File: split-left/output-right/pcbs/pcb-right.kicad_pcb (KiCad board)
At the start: 2 copper layers, 243.1 x 138 mm, 113 parts

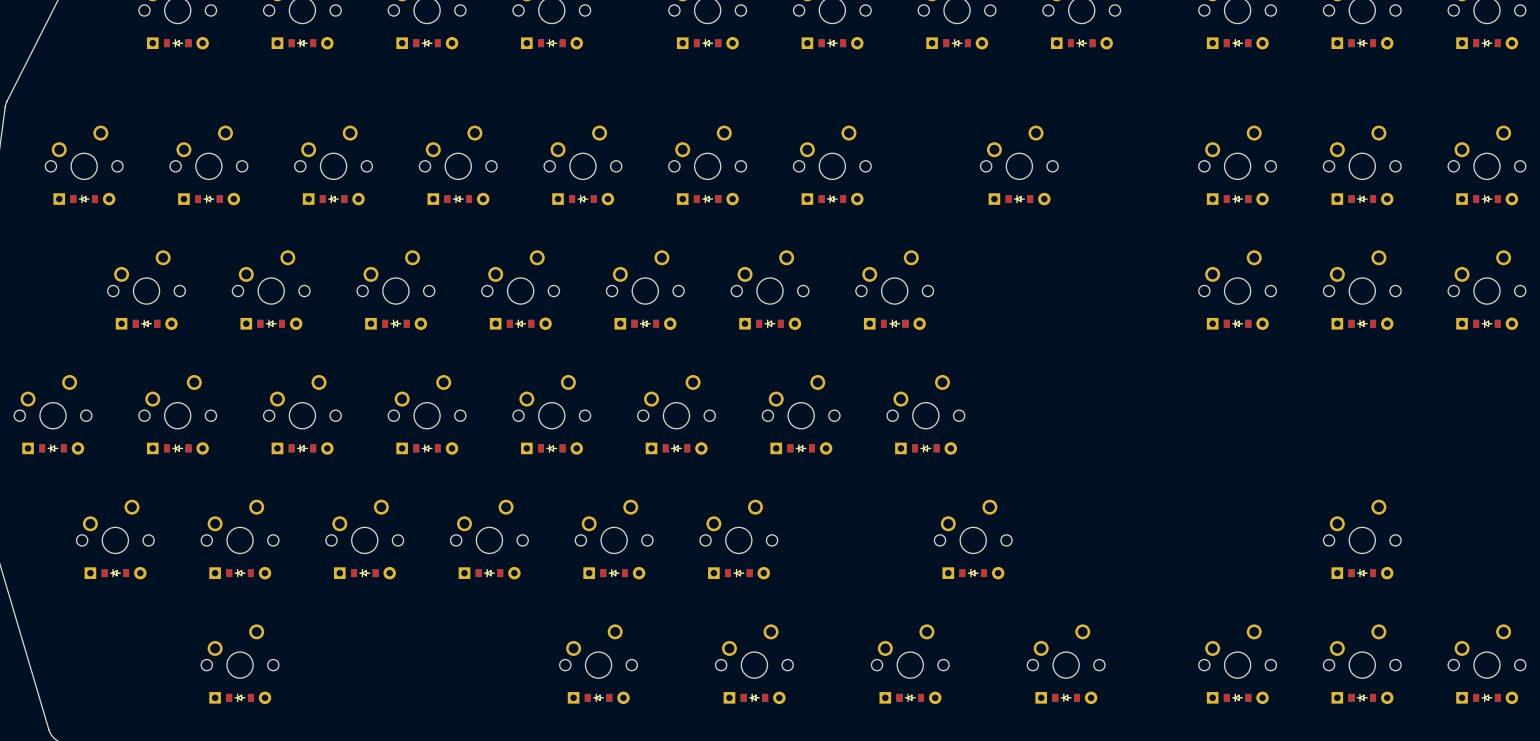
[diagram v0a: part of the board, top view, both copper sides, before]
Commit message: On the right hand keeb, adjusted the net cols for the bottom 2 rows to fix the matrix
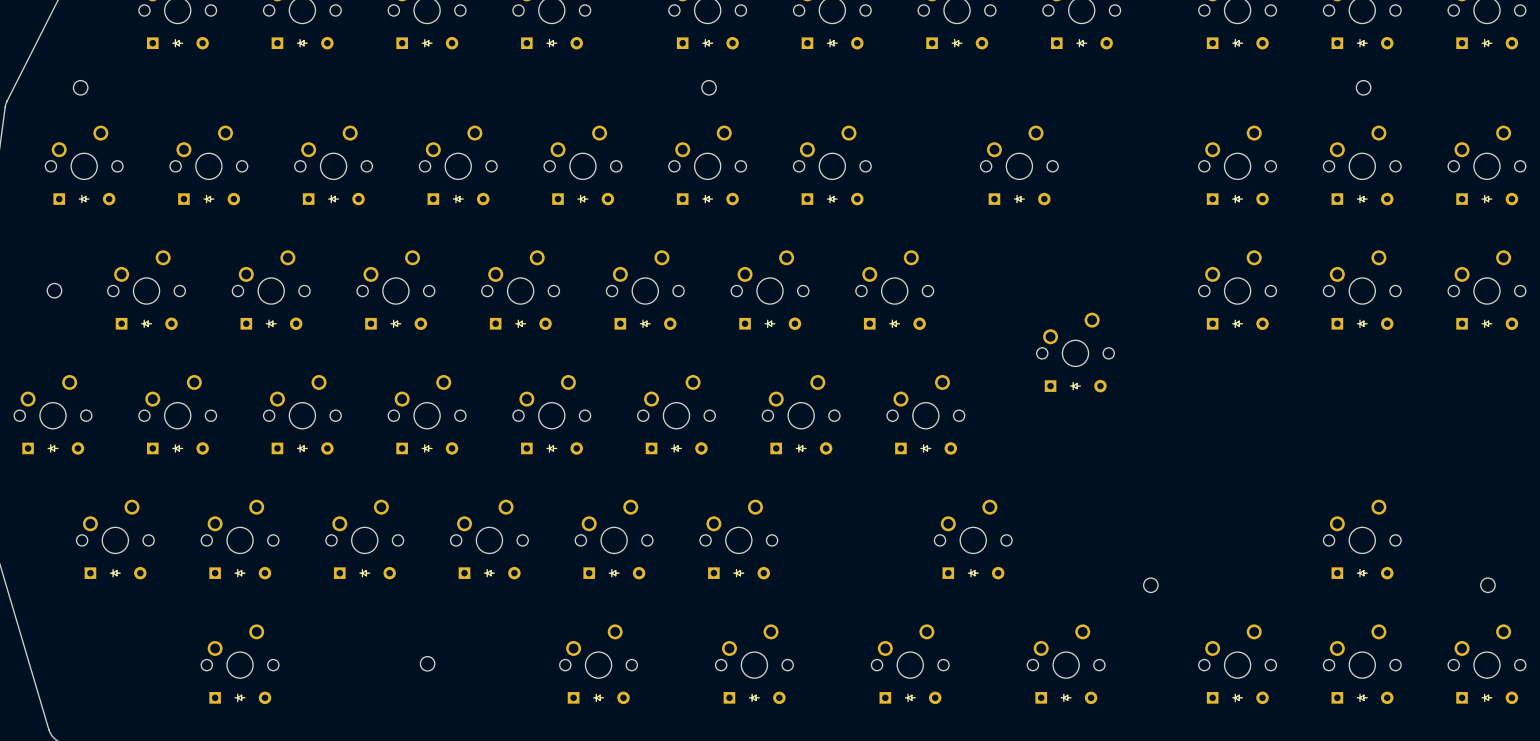
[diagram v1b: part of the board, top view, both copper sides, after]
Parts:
- added D57: , ComboDiode, F.Cu at (348.9, 130.0)
- added MH1: , ceoloide:mounting_hole_npth, F.Cu at (134.0, 113.0)
- added MH2: , ceoloide:mounting_hole_npth, F.Cu at (230.0, 113.0)
- added MH3: , ceoloide:mounting_hole_npth, F.Cu at (330.0, 113.0)
- added MH4: , ceoloide:mounting_hole_npth, F.Cu at (349.0, 189.0)
- added MH5: , ceoloide:mounting_hole_npth, F.Cu at (297.5, 189.0)
- added MH6: , ceoloide:mounting_hole_npth, F.Cu at (187.0, 201.0)
- added MH7: , ceoloide:mounting_hole_npth, F.Cu at (130.0, 144.0)
- added S57: , MX, F.Cu at (348.9, 125.0)
- moved D50 78.5 mm to (310.8, 130.0)
- moved D54 78.5 mm to (329.8, 130.0)
- moved S50 78.5 mm to (310.8, 125.0)
- moved S54 78.5 mm to (329.8, 125.0)
- moved D48 57.2 mm to (310.8, 206.2)
- moved D55 57.2 mm to (348.9, 206.2)
- moved S48 57.2 mm to (310.8, 201.2)
- moved S55 57.2 mm to (348.9, 201.2)
- moved D47 53.7 mm to (286.0, 158.6)
- moved S47 53.7 mm to (286.0, 153.6)
- moved D52 38.1 mm to (329.8, 187.1)
- moved S52 38.1 mm to (329.8, 182.1)
- moved D49 19.1 mm to (310.8, 149.0)
- moved D51 19.1 mm to (329.8, 206.2)
- moved D53 19.1 mm to (329.8, 149.0)
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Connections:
- D1 pad 1: (no net) -> B5
- D10 pad 1: (no net) -> B6
- D11 pad 1: (no net) -> B6
- D12 pad 1: (no net) -> B6
- D13 pad 1: (no net) -> B6
- D14 pad 1: (no net) -> B6
- D15 pad 1: (no net) -> B6
- D16 pad 1: (no net) -> B7
- D17 pad 1: (no net) -> B7
- D18 pad 1: (no net) -> B7
- D19 pad 1: (no net) -> B7
- D2 pad 1: (no net) -> B5
- D20 pad 1: (no net) -> B7
- D21 pad 1: (no net) -> B7
- D22 pad 1: (no net) -> B7
- D23 pad 1: (no net) -> B7
- D24 pad 1: (no net) -> B8
- D25 pad 1: (no net) -> B8
- D26 pad 1: (no net) -> B8
- D27 pad 1: (no net) -> B8
- D28 pad 1: (no net) -> B8
- D29 pad 1: (no net) -> B8
- D3 pad 1: (no net) -> B5
- D30 pad 1: (no net) -> B8
- D31 pad 1: (no net) -> B4
- D32 pad 1: (no net) -> B4
- D33 pad 1: (no net) -> B4
- D34 pad 1: (no net) -> B4
- D35 pad 1: (no net) -> B4
- D36 pad 1: (no net) -> B4
- D37 pad 1: (no net) -> B4
- D38 pad 1: (no net) -> B4
- D39 pad 1: (no net) -> B4
- D4 pad 1: (no net) -> B5
- D40 pad 1: (no net) -> B4
- D41 pad 1: (no net) -> B4
- D42 pad 1: (no net) -> B9
- D43 pad 1: (no net) -> B9
- D44 pad 1: (no net) -> B9
- D45 pad 1: (no net) -> B9
- D46 pad 1: (no net) -> B9
- D47 pad 1: (no net) -> B6
- D47 pad 2: left_arrowLower -> only_only
- D48 pad 1: (no net) -> B9
- D48 pad 2: left_delRow -> left_arrowLower
- D49 pad 1: (no net) -> B6
- D49 pad 2: left_insertRow -> left_delRow
- D5 pad 1: (no net) -> B5
- D50 pad 1: (no net) -> B5
- D50 pad 2: middle_arrowLower -> left_insertRow
- D51 pad 1: (no net) -> B9
- D51 pad 2: middle_arrowUpper -> middle_arrowLower
- D52 pad 1: (no net) -> B8
- D52 pad 2: middle_delRow -> middle_arrowUpper
- D53 pad 1: (no net) -> B6
- D53 pad 2: middle_insertRow -> middle_delRow
- D54 pad 1: (no net) -> B5
- D54 pad 2: right_arrowLower -> middle_insertRow
- D55 pad 1: (no net) -> B9
- D55 pad 2: right_delRow -> right_arrowLower
- D56 pad 1: (no net) -> B6
- D56 pad 2: right_insertRow -> right_delRow
- D6 pad 1: (no net) -> B5
- D7 pad 1: (no net) -> B5
- D8 pad 1: (no net) -> B5
- D9 pad 1: (no net) -> B6
- S1 pad 1: (no net) -> A4
- S10 pad 1: (no net) -> A5
- S11 pad 1: (no net) -> A6
- S12 pad 1: (no net) -> A7
- S13 pad 1: (no net) -> C13
- S14 pad 1: (no net) -> C14
- S15 pad 1: (no net) -> C15
- S16 pad 1: (no net) -> A4
- S17 pad 1: (no net) -> A5
- S18 pad 1: (no net) -> A6
- S19 pad 1: (no net) -> A7
- S2 pad 1: (no net) -> A5
- S20 pad 1: (no net) -> C13
- S21 pad 1: (no net) -> C14
- S22 pad 1: (no net) -> C15
- S23 pad 1: (no net) -> A0
- S24 pad 1: (no net) -> A4
- S25 pad 1: (no net) -> A5
- S26 pad 1: (no net) -> A6
- S27 pad 1: (no net) -> A7
- S28 pad 1: (no net) -> C13
- S29 pad 1: (no net) -> C14
- S3 pad 1: (no net) -> A6
- S30 pad 1: (no net) -> A0
- S31 pad 1: (no net) -> A4
- S32 pad 1: (no net) -> A5
- S33 pad 1: (no net) -> A6
- S34 pad 1: (no net) -> A7
- S35 pad 1: (no net) -> C13
- S36 pad 1: (no net) -> C14
- S37 pad 1: (no net) -> C15
- S38 pad 1: (no net) -> A0
- S39 pad 1: (no net) -> A1
- S4 pad 1: (no net) -> A7
- S40 pad 1: (no net) -> A2
- S41 pad 1: (no net) -> A3
- S42 pad 1: (no net) -> A5
- S43 pad 1: (no net) -> C13
- S44 pad 1: (no net) -> C14
- S45 pad 1: (no net) -> C15
- S46 pad 1: (no net) -> A0
- S47 pad 1: (no net) -> A0
- S47 pad 2: left_arrowLower -> only_only
- S48 pad 1: (no net) -> A1
- S48 pad 2: left_delRow -> left_arrowLower
- S49 pad 1: (no net) -> A1
- S49 pad 2: left_insertRow -> left_delRow
- S5 pad 1: (no net) -> C13
- S50 pad 1: (no net) -> A1
- S50 pad 2: middle_arrowLower -> left_insertRow
- S51 pad 1: (no net) -> A2
- S51 pad 2: middle_arrowUpper -> middle_arrowLower
- S52 pad 1: (no net) -> A2
- S52 pad 2: middle_delRow -> middle_arrowUpper
- S53 pad 1: (no net) -> A2
- S53 pad 2: middle_insertRow -> middle_delRow
- S54 pad 1: (no net) -> A2
- S54 pad 2: right_arrowLower -> middle_insertRow
- S55 pad 1: (no net) -> A3
- S55 pad 2: right_delRow -> right_arrowLower
- S56 pad 1: (no net) -> A3
- S56 pad 2: right_insertRow -> right_delRow
- S6 pad 1: (no net) -> C14
- S7 pad 1: (no net) -> C15
- S8 pad 1: (no net) -> A0
- S9 pad 1: (no net) -> A4
